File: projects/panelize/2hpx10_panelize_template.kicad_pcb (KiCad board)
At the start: 2 copper layers, 113 x 124 mm, 50 parts

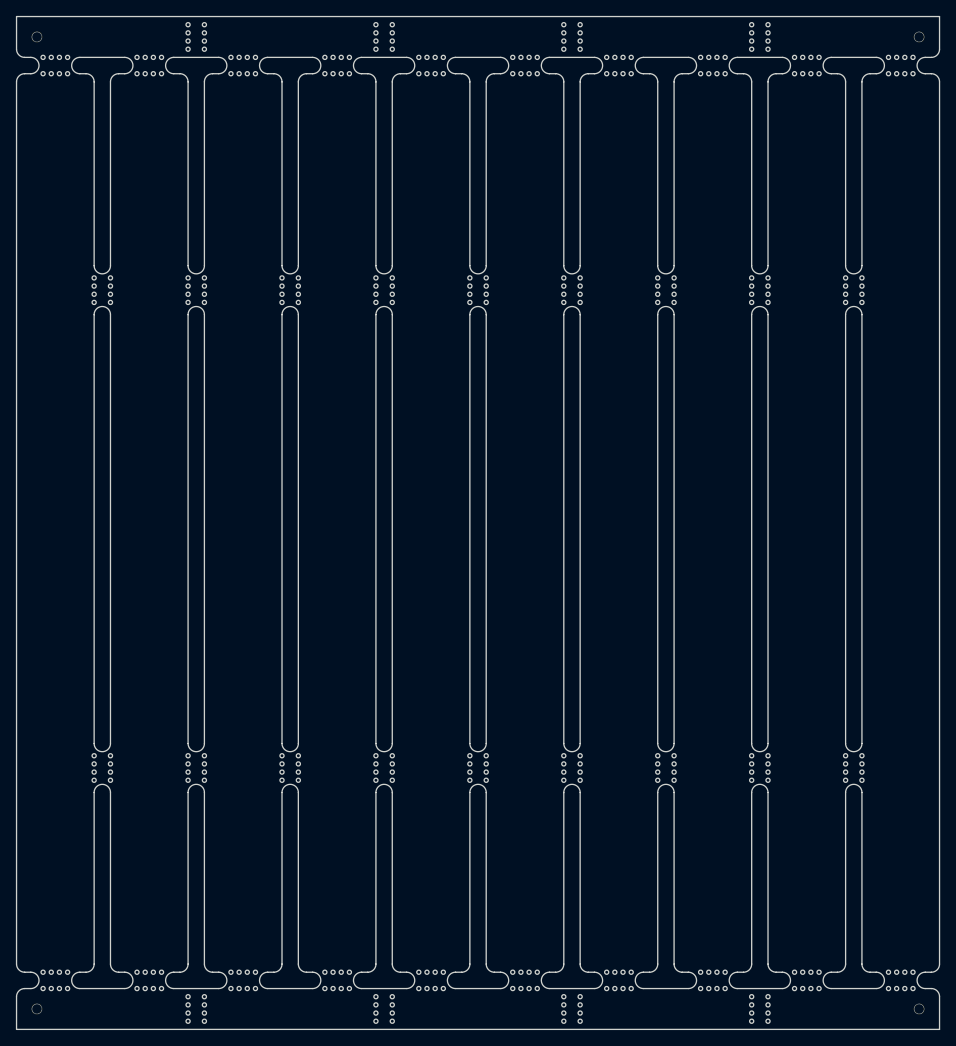
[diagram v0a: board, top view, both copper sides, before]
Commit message: update 2hp panelize template
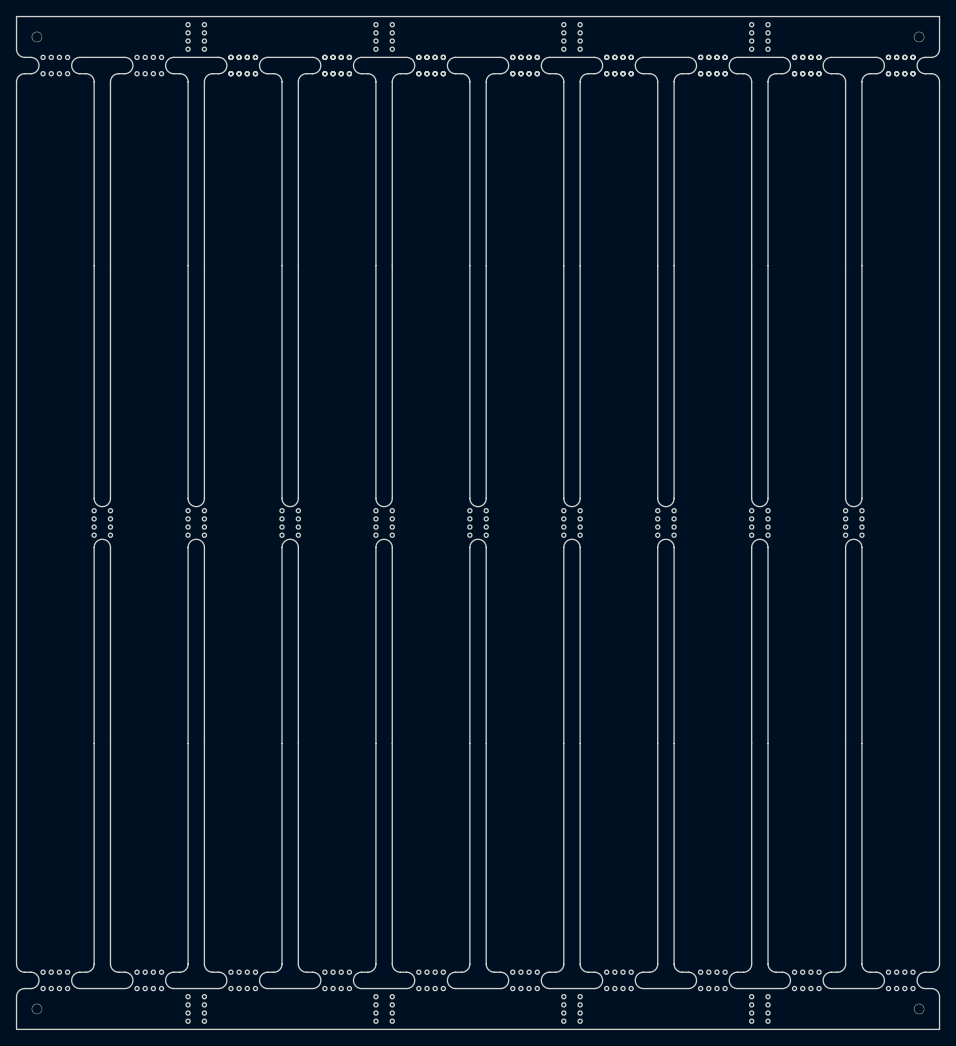
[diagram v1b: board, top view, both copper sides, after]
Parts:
- removed the REF** at (106.5, 76.5)
- removed the REF** at (95.0, 76.5)
- removed the REF** at (72.0, 76.5)
- removed the REF** at (141.0, 76.5)
- removed the REF** at (118.0, 76.5)
- removed the REF** at (83.5, 76.5)
- removed the REF** at (129.5, 76.5)
- removed the REF** at (152.5, 76.5)
- removed the REF** at (60.5, 135.0)
- removed the REF** at (141.0, 135.0)
- removed the REF** at (129.5, 135.0)
- removed the REF** at (118.0, 135.0)
- removed the REF** at (72.0, 135.0)
- removed the REF** at (152.5, 135.0)
- removed the REF** at (95.0, 135.0)
- removed the REF** at (83.5, 135.0)
- removed the REF** at (106.5, 135.0)
- added REF**: PANELIZE_MOUSE_BITES, kicadlib:PANELIZE_MOUSE_BITES, F.Cu at (152.5, 105.0)
- added REF**: PANELIZE_MOUSE_BITES, kicadlib:PANELIZE_MOUSE_BITES, F.Cu at (146.8, 49.0)
- added REF**: PANELIZE_MOUSE_BITES, kicadlib:PANELIZE_MOUSE_BITES, F.Cu at (135.2, 49.0)
- added REF**: PANELIZE_MOUSE_BITES, kicadlib:PANELIZE_MOUSE_BITES, F.Cu at (123.8, 49.0)
- added REF**: PANELIZE_MOUSE_BITES, kicadlib:PANELIZE_MOUSE_BITES, F.Cu at (112.2, 49.0)
- added REF**: PANELIZE_MOUSE_BITES, kicadlib:PANELIZE_MOUSE_BITES, F.Cu at (100.8, 49.0)
- added REF**: PANELIZE_MOUSE_BITES, kicadlib:PANELIZE_MOUSE_BITES, F.Cu at (89.2, 49.0)
- added REF**: PANELIZE_MOUSE_BITES, kicadlib:PANELIZE_MOUSE_BITES, F.Cu at (77.8, 49.0)
- added REF**: PANELIZE_MOUSE_BITES, kicadlib:PANELIZE_MOUSE_BITES, F.Cu at (141.0, 105.0)
- added REF**: PANELIZE_MOUSE_BITES, kicadlib:PANELIZE_MOUSE_BITES, F.Cu at (129.5, 105.0)
- added REF**: PANELIZE_MOUSE_BITES, kicadlib:PANELIZE_MOUSE_BITES, F.Cu at (118.0, 105.0)
- added REF**: PANELIZE_MOUSE_BITES, kicadlib:PANELIZE_MOUSE_BITES, F.Cu at (106.5, 105.0)
- added REF**: PANELIZE_MOUSE_BITES, kicadlib:PANELIZE_MOUSE_BITES, F.Cu at (95.0, 105.0)
- added REF**: PANELIZE_MOUSE_BITES, kicadlib:PANELIZE_MOUSE_BITES, F.Cu at (83.5, 105.0)
- added REF**: PANELIZE_MOUSE_BITES, kicadlib:PANELIZE_MOUSE_BITES, F.Cu at (72.0, 105.0)
- added REF**: PANELIZE_MOUSE_BITES, kicadlib:PANELIZE_MOUSE_BITES, F.Cu at (158.2, 49.0)
- moved REF** 28.5 mm to (60.5, 105.0)
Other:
- outline, holes or cut-outs redrawn

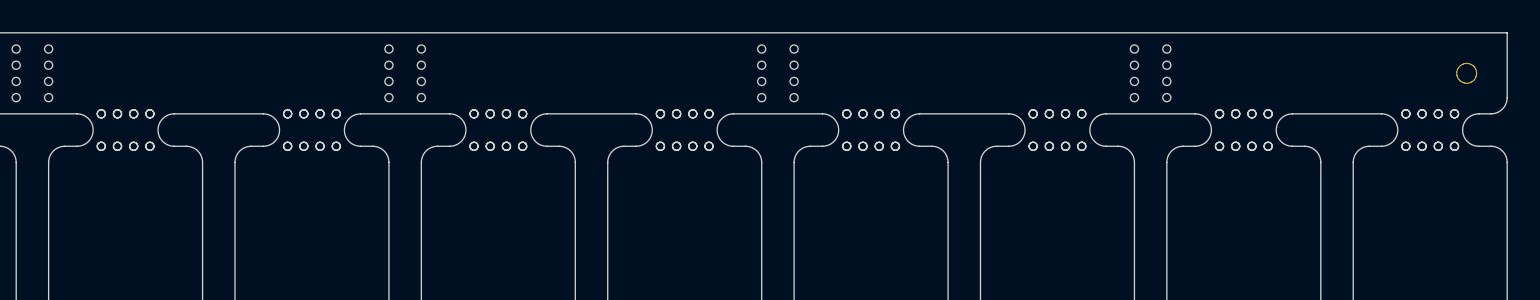
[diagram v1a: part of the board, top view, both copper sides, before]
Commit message: fix panelize pcb layout
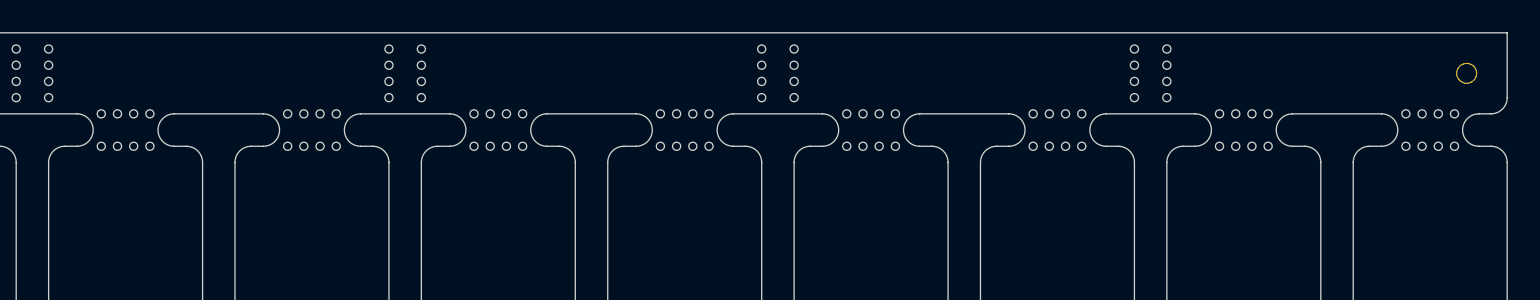
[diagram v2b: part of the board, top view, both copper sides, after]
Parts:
- removed the REF** at (123.8, 49.0)
- removed the REF** at (100.8, 49.0)
- removed the REF** at (146.8, 49.0)
- removed the REF** at (112.2, 49.0)
- removed the REF** at (89.2, 49.0)
- removed the REF** at (77.8, 49.0)
- removed the REF** at (135.2, 49.0)
- removed the REF** at (158.2, 49.0)
